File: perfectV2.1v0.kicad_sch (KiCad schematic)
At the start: 5 parts, among them U1 Teensy4.1

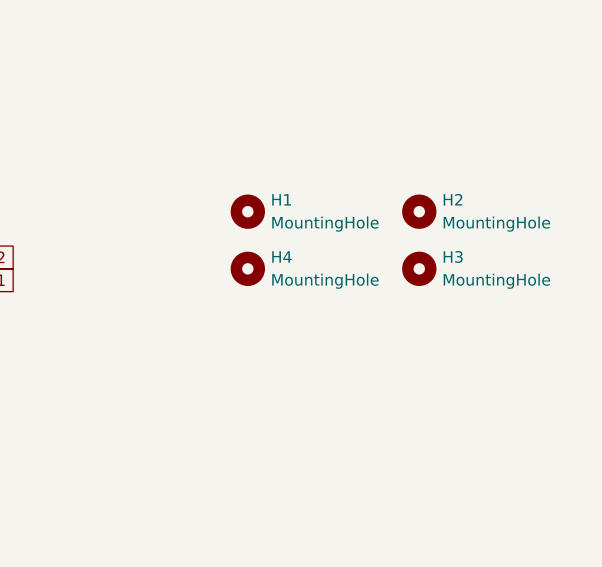
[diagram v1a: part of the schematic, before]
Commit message: Assigned fp to mounting holes, removed datasheet fields
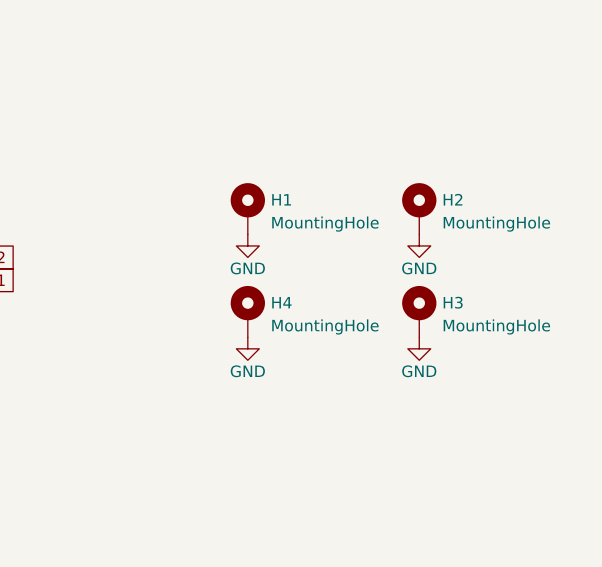
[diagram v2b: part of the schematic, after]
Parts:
- H1, H2, H3, H4: footprint (none) -> MountingHole:MountingHole_4.3mm_M4_Pad; symbol Mechanical:MountingHole -> Mechanical:MountingHole_Pad
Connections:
- net GND: now also H1.1, H2.1, H3.1, H4.1
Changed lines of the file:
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@@
       (effects (font (size 1.27 1.27)) hide)
     )
-    (property "Datasheet" "" (id 3) (at 111.76 77.47 0)
+    (property "Datasheet" "~" (id 3) (at 111.76 77.47 0)
       (effects (font (size 1.27 1.27)) hide)
     )
@@
     (pin "1")
   )
-  (symbol (lib_id "Mechanical:MountingHole") (at 215.9 66.04 0) (unit 1)
+  (symbol (lib_id "Mechanical:MountingHole_Pad") (at 215.9 66.04 0) (unit 1)
     (in_bom yes) (on_board yes) (fields_autoplaced)
     (property "Reference" "H2" (id 0) (at 218.44 64.7699 0)
@@
       (effects (font (size 1.27 1.27)) (justify left))
     )
-    (property "Footprint" "" (id 2) (at 215.9 66.04 0)
+    (property "Footprint" "MountingHole:MountingHole_4.3mm_M4_Pad" (id 2) (at 215.9 66.04 0)
       (effects (font (size 1.27 1.27)) hide)
     )
@@
       (effects (font (size 1.27 1.27)) hide)
     )
+    (pin "1")
+  )
+  (symbol (lib_id "power:GND") (at 196.85 80.01 0) (unit 1)
+    (in_bom yes) (on_board yes)
+    (property "Reference" "#PWR?" (id 0) (at 196.85 86.36 0)
+      (effects (font (size 1.27 1.27)) hide)
+    )
+    (property "Value" "GND" (id 1) (at 196.85 83.82 0))
+    (property "Footprint" "" (id 2) (at 196.85 80.01 0)
+      (effects (font (size 1.27 1.27)) hide)
+    )
+    (property "Datasheet" "" (id 3) (at 196.85 80.01 0)
+      (effects (font (size 1.27 1.27)) hide)
+    )
+    (pin "1")
+  )
+  (symbol (lib_id "power:GND") (at 196.85 68.58 0) (unit 1)
+    (in_bom yes) (on_board yes)
+    (property "Reference" "#PWR?" (id 0) (at 196.85 74.93 0)
+      (effects (font (size 1.27 1.27)) hide)
+    )
+    (property "Value" "GND" (id 1) (at 196.85 72.39 0))
+    (property "Footprint" "" (id 2) (at 196.85 68.58 0)
+      (effects (font (size 1.27 1.27)) hide)
+    )
+    (property "Datasheet" "" (id 3) (at 196.85 68.58 0)
+      (effects (font (size 1.27 1.27)) hide)
+    )
+    (pin "1")
+  )
+  (symbol (lib_id "power:GND") (at 215.9 68.58 0) (unit 1)
+    (in_bom yes) (on_board yes)
+    (property "Reference" "#PWR?" (id 0) (at 215.9 74.93 0)
+      (effects (font (size 1.27 1.27)) hide)
+    )
+    (property "Value" "GND" (id 1) (at 215.9 72.39 0))
+    (property "Footprint" "" (id 2) (at 215.9 68.58 0)
+      (effects (font (size 1.27 1.27)) hide)
+    )
+    (property "Datasheet" "" (id 3) (at 215.9 68.58 0)
+      (effects (font (size 1.27 1.27)) hide)
+    )
+    (pin "1")
+  )
+  (symbol (lib_id "power:GND") (at 215.9 80.01 0) (unit 1)
+    (in_bom yes) (on_board yes)
+    (property "Reference" "#PWR?" (id 0) (at 215.9 86.36 0)
+      (effects (font (size 1.27 1.27)) hide)
+    )
+    (property "Value" "GND" (id 1) (at 215.9 83.82 0))
+    (property "Footprint" "" (id 2) (at 215.9 80.01 0)
+      (effects (font (size 1.27 1.27)) hide)
+    )
+    (property "Datasheet" "" (id 3) (at 215.9 80.01 0)
+      (effects (font (size 1.27 1.27)) hide)
+    )
+    (pin "1")
   )
   (symbol (lib_id "power:VDD") (at 154.94 33.02 270) (unit 1)
@@
     (pin "1")
   )
-  (symbol (lib_id "Mechanical:MountingHole") (at 215.9 72.39 0) (unit 1)
+  (symbol (lib_id "Mechanical:MountingHole_Pad") (at 215.9 77.47 0) (unit 1)
     (in_bom yes) (on_board yes) (fields_autoplaced)
-    (property "Reference" "H3" (id 0) (at 218.44 71.1199 0)
+    (property "Reference" "H3" (id 0) (at 218.44 76.1999 0)
       (effects (font (size 1.27 1.27)) (justify left))
     )
-    (property "Value" "MountingHole" (id 1) (at 218.44 73.6599 0)
+    (property "Value" "MountingHole" (id 1) (at 218.44 78.7399 0)
       (effects (font (size 1.27 1.27)) (justify left))
     )
-    (property "Footprint" "" (id 2) (at 215.9 72.39 0)
-      (effects (font (size 1.27 1.27)) hide)
-    )
-    (property "Datasheet" "~" (id 3) (at 215.9 72.39 0)
-      (effects (font (size 1.27 1.27)) hide)
-    )
-  )
-  (symbol (lib_id "Mechanical:MountingHole") (at 196.85 66.04 0) (unit 1)
+    (property "Footprint" "MountingHole:MountingHole_4.3mm_M4_Pad" (id 2) (at 215.9 77.47 0)
+      (effects (font (size 1.27 1.27)) hide)
+    )
+    (property "Datasheet" "~" (id 3) (at 215.9 77.47 0)
+      (effects (font (size 1.27 1.27)) hide)
+    )
+    (pin "1")
+  )
+  (symbol (lib_id "Mechanical:MountingHole_Pad") (at 196.85 66.04 0) (unit 1)
     (in_bom yes) (on_board yes) (fields_autoplaced)
     (property "Reference" "H1" (id 0) (at 199.39 64.7699 0)
@@
       (effects (font (size 1.27 1.27)) (justify left))
     )
-    (property "Footprint" "" (id 2) (at 196.85 66.04 0)
+    (property "Footprint" "MountingHole:MountingHole_4.3mm_M4_Pad" (id 2) (at 196.85 66.04 0)
       (effects (font (size 1.27 1.27)) hide)
     )
@@
       (effects (font (size 1.27 1.27)) hide)
     )
+    (pin "1")
   )
   (symbol (lib_id "power:+3V3") (at 154.94 38.1 270) (unit 1)
@@
     (pin "1")
   )
-  (symbol (lib_id "Mechanical:MountingHole") (at 196.85 72.39 0) (unit 1)
+  (symbol (lib_id "Mechanical:MountingHole_Pad") (at 196.85 77.47 0) (unit 1)
     (in_bom yes) (on_board yes) (fields_autoplaced)
-    (property "Reference" "H4" (id 0) (at 199.39 71.1199 0)
+    (property "Reference" "H4" (id 0) (at 199.39 76.1999 0)
       (effects (font (size 1.27 1.27)) (justify left))
     )
-    (property "Value" "MountingHole" (id 1) (at 199.39 73.6599 0)
+    (property "Value" "MountingHole" (id 1) (at 199.39 78.7399 0)
       (effects (font (size 1.27 1.27)) (justify left))
     )
-    (property "Footprint" "" (id 2) (at 196.85 72.39 0)
-      (effects (font (size 1.27 1.27)) hide)
-    )
-    (property "Datasheet" "~" (id 3) (at 196.85 72.39 0)
-      (effects (font (size 1.27 1.27)) hide)
-    )
+    (property "Footprint" "MountingHole:MountingHole_4.3mm_M4_Pad" (id 2) (at 196.85 77.47 0)
+      (effects (font (size 1.27 1.27)) hide)
+    )
+    (property "Datasheet" "~" (id 3) (at 196.85 77.47 0)
+      (effects (font (size 1.27 1.27)) hide)
+    )
+    (pin "1")
   )
   (symbol (lib_id "power:GND") (at 90.17 33.02 270) (unit 1)
@@
       (reference "#PWR0234") (unit 1) (value "GND") (footprint "")
     )
+    (path "/559ee613-373d-468b-8df3-d3159516fbee"
+      (reference "#PWR?") (unit 1) (value "GND") (footprint "")
+    )
+    (path "/587c1643-27ae-411f-aea8-4d7a7d767ced"
+      (reference "#PWR?") (unit 1) (value "GND") (footprint "")
+    )
+    (path "/63b75572-6f9a-450f-a53d-8b3945dcc770"
+      (reference "#PWR?") (unit 1) (value "GND") (footprint "")
+    )
+    (path "/6a08b53d-e63a-4a5d-a2d9-f4991e44c3cd"
+      (reference "#PWR?") (unit 1) (value "GND") (footprint "")
+    )
     (path "/00000000-0000-0000-0000-00005cd191f5/00000000-0000-0000-0000-00005cfe4b9e"
       (reference "A1") (unit 1) (value "Pololu_Breakout_DRV8825") (footprint "Module:Pololu_Breakout-16_15.2x20.3mm")
@@
     )
     (path "/a4d2a016-50eb-46d0-bd74-e089fc8fcff9"
-      (reference "H1") (unit 1) (value "MountingHole") (footprint "")
+      (reference "H1") (unit 1) (value "MountingHole") (footprint "MountingHole:MountingHole_4.3mm_M4_Pad")
     )
     (path "/54f58726-c5fb-4653-b81c-88d921177a57"
-      (reference "H2") (unit 1) (value "MountingHole") (footprint "")
+      (reference "H2") (unit 1) (value "MountingHole") (footprint "MountingHole:MountingHole_4.3mm_M4_Pad")
     )
     (path "/95f7b234-79b3-4962-a9a1-f8d83f96690b"
-      (reference "H3") (unit 1) (value "MountingHole") (footprint "")
+      (reference "H3") (unit 1) (value "MountingHole") (footprint "MountingHole:MountingHole_4.3mm_M4_Pad")
     )
     (path "/c9523306-be98-4c03-8f31-4177d2b3b8c1"
-      (reference "H4") (unit 1) (value "MountingHole") (footprint "")
+      (reference "H4") (unit 1) (value "MountingHole") (footprint "MountingHole:MountingHole_4.3mm_M4_Pad")
     )
     (path "/00000000-0000-0000-0000-00006257c513/00000000-0000-0000-0000-000062600b64"
